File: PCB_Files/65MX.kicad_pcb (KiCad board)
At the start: 2 copper layers, 303.8 x 94.2 mm, 135 parts, among them J1 jst_sh, SW1 NRST, SW2 NRST, U1 STM32F072CBTx, U2 SRV05-4, U3 XC6206PxxxMR

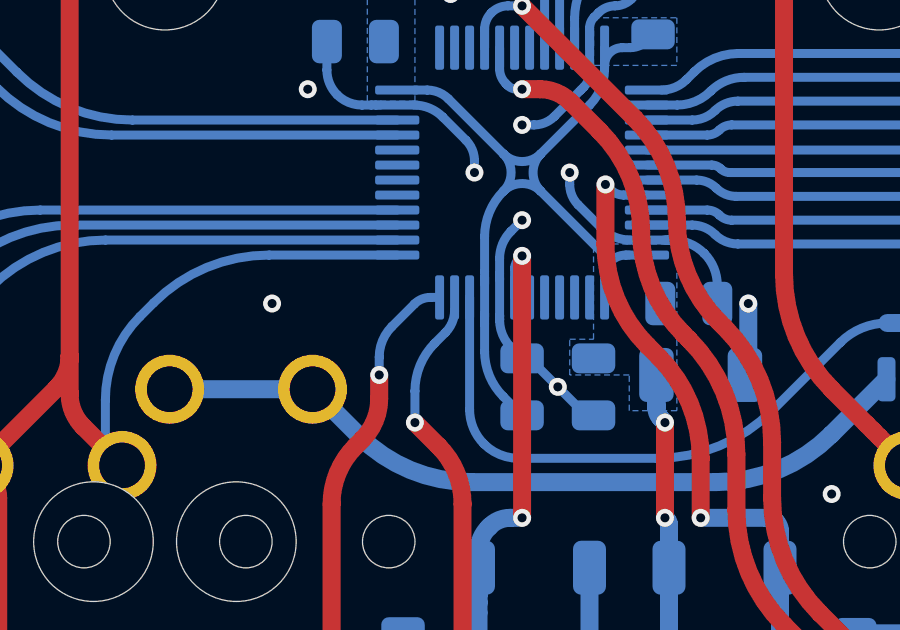
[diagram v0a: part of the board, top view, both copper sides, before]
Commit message: added firmware
added the qmk firmware files to the repo
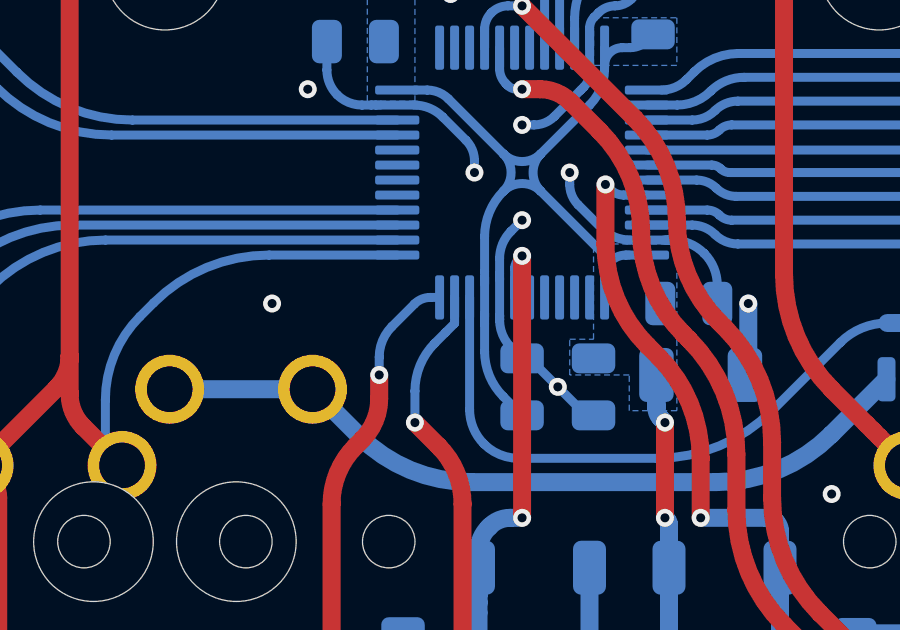
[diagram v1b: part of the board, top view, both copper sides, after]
